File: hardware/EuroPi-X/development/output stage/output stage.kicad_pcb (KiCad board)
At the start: 2 copper layers, 22.9 x 15.2 mm, 27 parts, among them J1 Conn_01x06_Pin, J2 Conn_01x06_Pin, U1 TL074

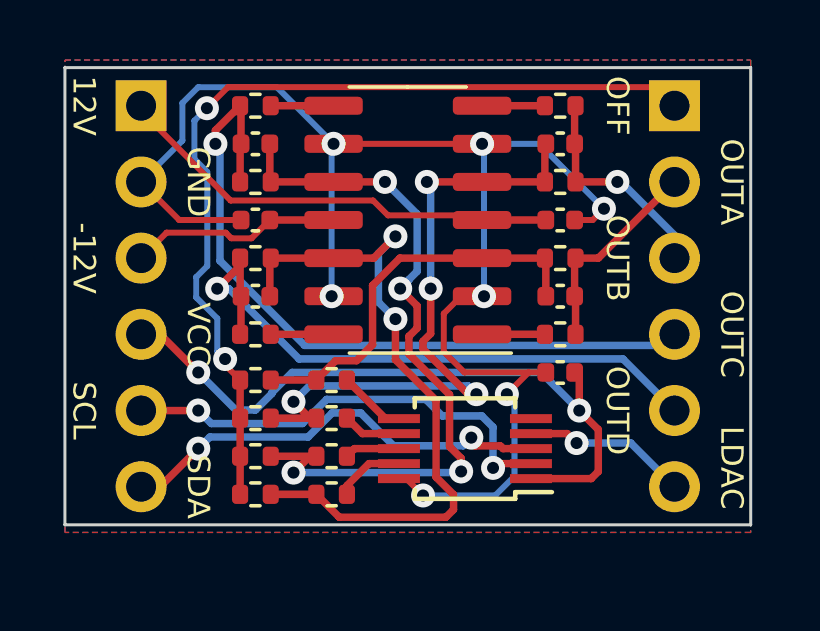
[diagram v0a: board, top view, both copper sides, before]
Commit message: save output stage
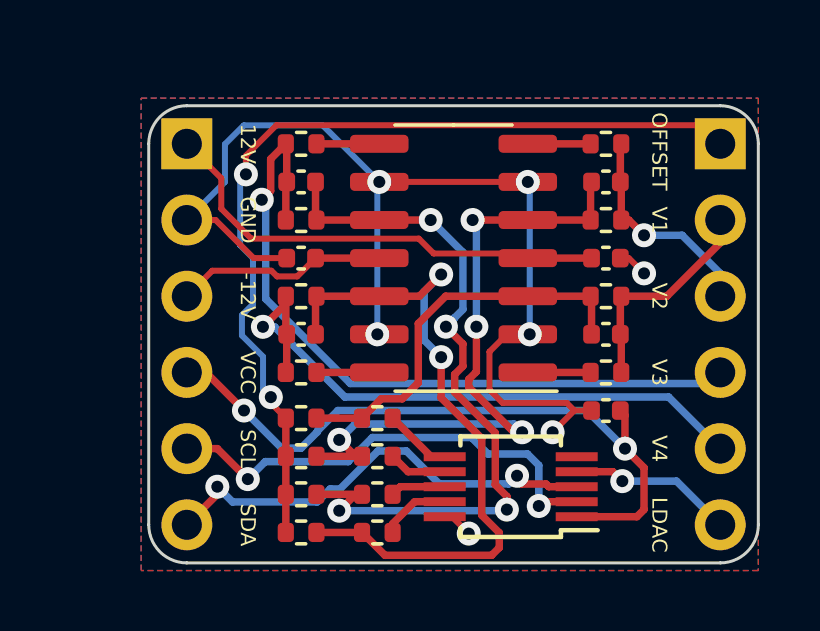
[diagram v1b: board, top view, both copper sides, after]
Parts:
- moved R10 1.98 mm to (7.87, 13.0)
- moved R9 1.98 mm to (5.33, 13.0)
- moved DAC1 1.98 mm to (12.3, 12.7)
- moved J1 1.98 mm to (1.52, 1.27)
- moved R14 1.98 mm to (7.87, 14.2)
- moved R2 1.98 mm to (7.87, 10.4)
- moved R6 1.98 mm to (7.87, 11.7)
- moved C2 1.98 mm to (15.5, 7.62)
- moved C4 1.98 mm to (5.33, 2.54)
- moved C5 1.98 mm to (5.33, 7.62)
- moved C7 1.98 mm to (5.33, 5.08)
- moved R11 1.98 mm to (5.33, 3.81)
- moved R12 1.98 mm to (5.33, 1.27)
- moved R16 1.98 mm to (5.33, 8.89)
- moved R4 1.98 mm to (15.5, 8.89)
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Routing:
- net Earth: track 49.1 -> 37.9 mm
- net /SDA: track 14.8 -> 15.4 mm
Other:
- board size 22.9 x 15.2 mm -> 20.3 x 15.2 mm
- board text added: "OFFSET"
- board text added: "V1"
- board text added: "V2"
- board text added: "V3"
- board text added: "V4"
- board text added: "europi-x output stage v1.0"
- board text added: "www.allensynthesis.co.uk"
- board text removed: "OFF"
- board text removed: "OUTA"
- board text removed: "OUTB"
- board text removed: "OUTC"
- board text removed: "OUTD"
